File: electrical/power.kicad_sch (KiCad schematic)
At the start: 67 parts

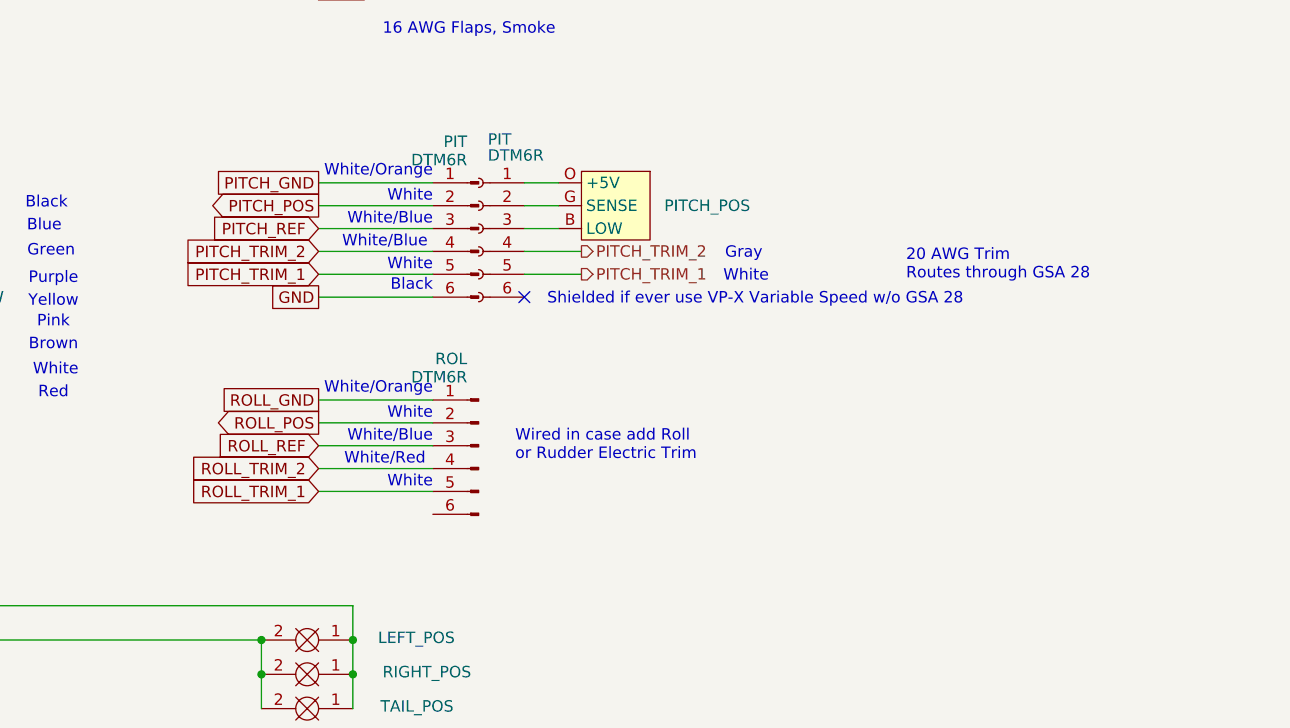
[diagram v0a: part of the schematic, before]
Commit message: Added Rudder Trim and Ray Allen T3 Servo Type.
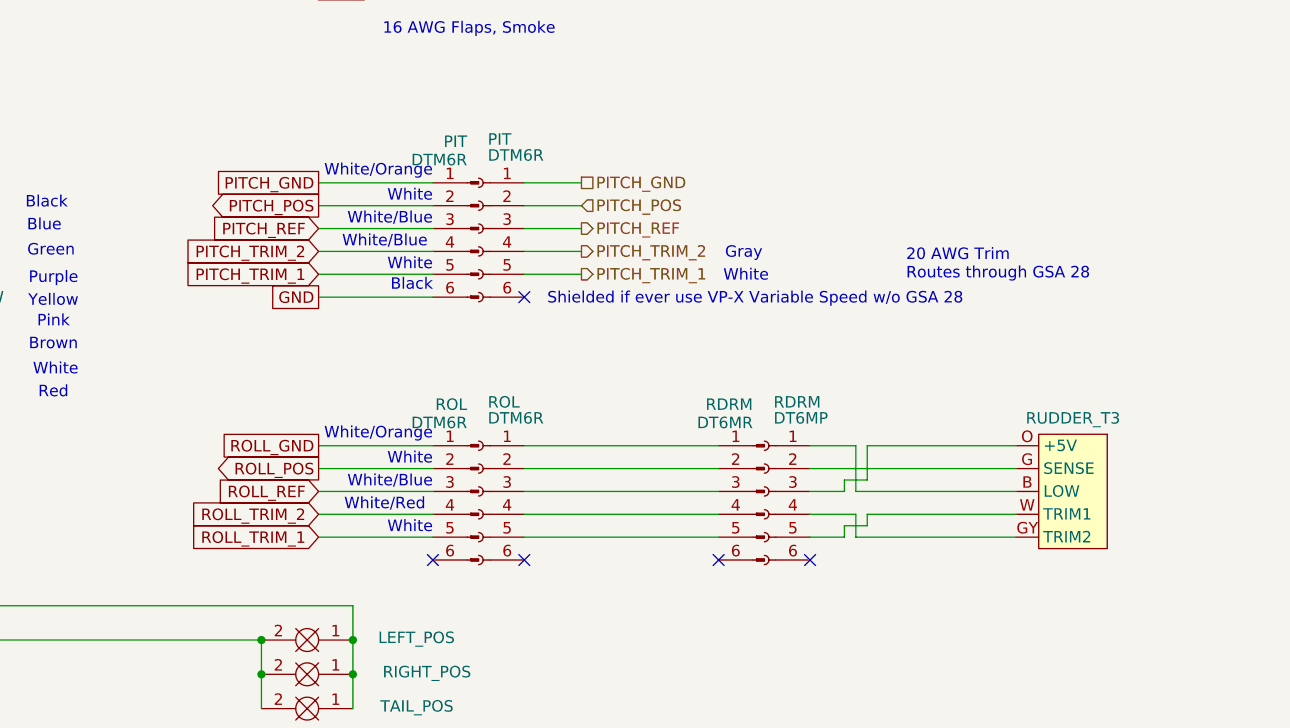
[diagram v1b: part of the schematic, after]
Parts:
- removed PITCH_POS: ~, symbol flyerx:Ray_Allen_POS-12
- added RDRM: DT6MR, symbol Connector:Conn_01x06_Pin
- added RDRM: DT6MP, symbol Connector:Conn_01x06_Socket
- added ROL: DTM6R, symbol Connector:Conn_01x06_Socket
- added RUDDER_T3: ~, symbol flyerx:Ray_Allen_T2/T3
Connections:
- net PITCH_GND: now also PIT.1 (Pin_1)
- net PITCH_POS: now also PIT.2 (Pin_2)
- net PITCH_REF: now also PIT.3 (Pin_3)
- new net: RDRM.1 (Pin_1), ROL.1 (Pin_1)
- new net: RDRM.2 (Pin_2), ROL.2 (Pin_2)
- new net: RDRM.3 (Pin_3), ROL.3 (Pin_3)
- new net: RDRM.4 (Pin_4), ROL.4 (Pin_4)
- new net: RDRM.5 (Pin_5), ROL.5 (Pin_5)
- new net: RDRM.1 (Pin_1), RUDDER_T3.B (LOW)
- new net: RDRM.2 (Pin_2), RUDDER_T3.G (SENSE)
- new net: RDRM.4 (Pin_4), RUDDER_T3.GY (TRIM2)
- new net: RDRM.3 (Pin_3), RUDDER_T3.O (+5V)
- new net: RDRM.5 (Pin_5), RUDDER_T3.W (TRIM1)
- no-connect marks 7 -> 11
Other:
- note removed: "Wired in case add Roll or Rudder Electric Trim"
- moved on the sheet: ROL

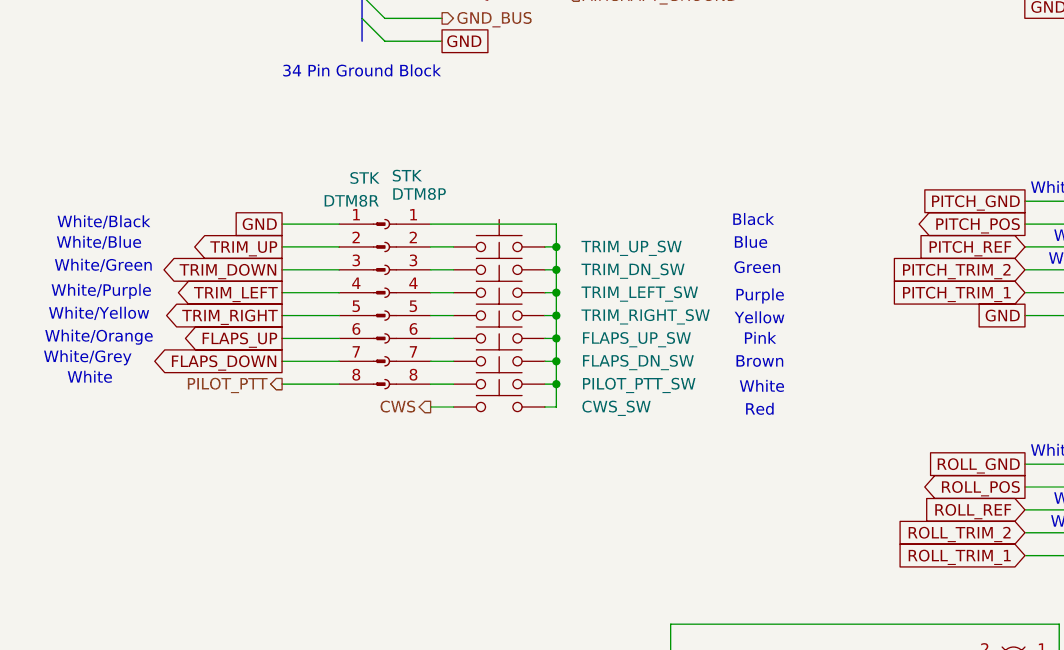
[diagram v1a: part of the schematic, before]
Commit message: Added connector to allow stick removal.
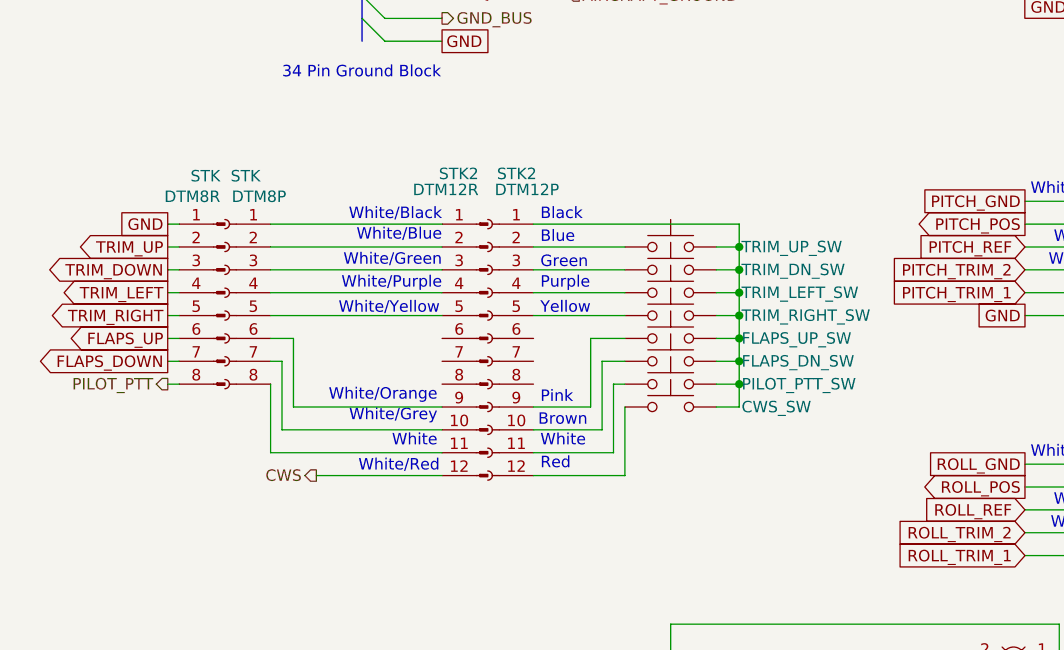
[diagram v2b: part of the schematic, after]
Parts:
- added STK2: DTM12R, symbol Connector:Conn_01x12_Pin
- added STK2: DTM12P, symbol Connector:Conn_01x12_Socket
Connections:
- net CWS: now also STK2.12 (Pin_12); no longer CWS_SW.1
- net at TRIM_UP_SW.1: now also STK2.2 (Pin_2); no longer STK.2 (Pin_2)
- net at CWS_SW.2, FLAPS_DN_SW.2, FLAPS_UP_SW.2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: now also STK2.1 (Pin_1); no longer STK.1 (Pin_1)
- net at TRIM_RIGHT_SW.1: now also STK2.5 (Pin_5); no longer STK.5 (Pin_5)
- net at FLAPS_DN_SW.1: now also STK2.10 (Pin_10); no longer STK.7 (Pin_7)
- net at TRIM_DN_SW.1: now also STK2.3 (Pin_3); no longer STK.3 (Pin_3)
- net at STK.6 (Pin_6): now also STK2.9 (Pin_9); no longer FLAPS_UP_SW.1
- net at STK.8 (Pin_8): now also STK2.11 (Pin_11); no longer PILOT_PTT_SW.1
- net at STK.4 (Pin_4): now also STK2.4 (Pin_4); no longer TRIM_LEFT_SW.1
- new net: CWS_SW.1, STK2.12 (Pin_12)
- new net: STK.1 (Pin_1), STK2.1 (Pin_1)
- new net: STK.7 (Pin_7), STK2.10 (Pin_10)
- new net: STK.2 (Pin_2), STK2.2 (Pin_2)
- new net: STK.3 (Pin_3), STK2.3 (Pin_3)
- new net: STK.5 (Pin_5), STK2.5 (Pin_5)
- new net: FLAPS_UP_SW.1, STK2.9 (Pin_9)
- new net: PILOT_PTT_SW.1, STK2.11 (Pin_11)
- new net: STK2.4 (Pin_4), TRIM_LEFT_SW.1
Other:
- moved on the sheet: CWS_SW, FLAPS_DN_SW, FLAPS_UP_SW, PILOT_PTT_SW, STK, TRIM_DN_SW, TRIM_LEFT_SW, TRIM_RIGHT_SW, TRIM_UP_SW

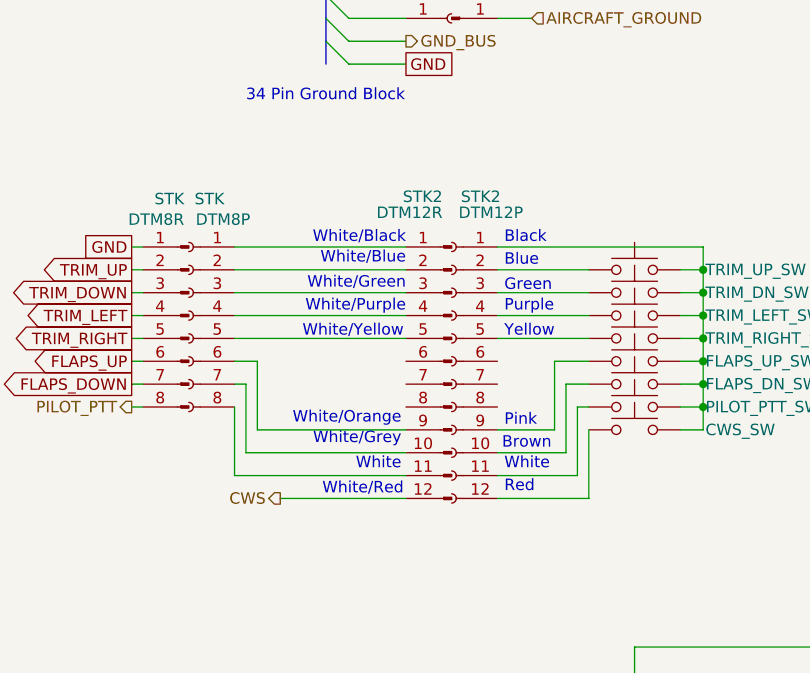
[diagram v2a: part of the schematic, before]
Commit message: Changed 12 connector to be populated in middle
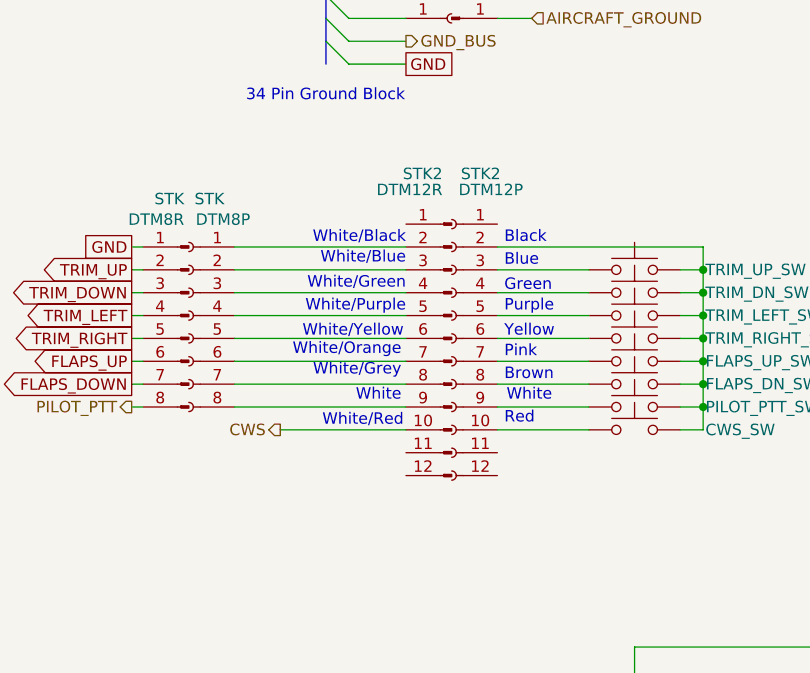
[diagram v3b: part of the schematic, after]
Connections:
- net CWS: now also STK2.10 (Pin_10); no longer STK2.12 (Pin_12)
- net at TRIM_UP_SW.1: now also STK2.3 (Pin_3); no longer STK2.2 (Pin_2)
- net at CWS_SW.2, FLAPS_DN_SW.2, FLAPS_UP_SW.2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: now also STK2.2 (Pin_2); no longer STK2.1 (Pin_1)
- net at CWS_SW.1: now also STK2.10 (Pin_10); no longer STK2.12 (Pin_12)
- net at TRIM_RIGHT_SW.1: now also STK2.6 (Pin_6); no longer STK2.5 (Pin_5)
- net at FLAPS_DN_SW.1: now also STK2.8 (Pin_8); no longer STK2.10 (Pin_10)
- net at TRIM_DN_SW.1: now also STK2.4 (Pin_4); no longer STK2.3 (Pin_3)
- net at STK2.1 (Pin_1): no longer STK.1 (Pin_1)
- net at STK.7 (Pin_7): now also STK2.8 (Pin_8); no longer STK2.10 (Pin_10)
- net at STK2.11 (Pin_11): no longer STK.8 (Pin_8)
- net at STK2.2 (Pin_2): now also STK.1 (Pin_1); no longer STK.2 (Pin_2)
- net at STK2.3 (Pin_3): now also STK.2 (Pin_2); no longer STK.3 (Pin_3)
- net at STK2.4 (Pin_4): now also STK.3 (Pin_3); no longer STK.4 (Pin_4)
- net at STK2.5 (Pin_5): now also STK.4 (Pin_4); no longer STK.5 (Pin_5)
- net at STK2.6 (Pin_6): now also STK.5 (Pin_5)
- net at STK2.7 (Pin_7): now also STK.6 (Pin_6)
- net at STK2.9 (Pin_9): now also STK.8 (Pin_8); no longer STK.6 (Pin_6)
- net at FLAPS_UP_SW.1: now also STK2.7 (Pin_7); no longer STK2.9 (Pin_9)
- net at PILOT_PTT_SW.1: now also STK2.9 (Pin_9); no longer STK2.11 (Pin_11)
- net at TRIM_LEFT_SW.1: now also STK2.5 (Pin_5); no longer STK2.4 (Pin_4)
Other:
- moved on the sheet: STK2
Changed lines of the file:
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@@
 	(text "Pink"
 		(exclude_from_sim no)
-		(at 68.072 297.434 0)
+		(at 68.072 289.814 0)
 		(effects
 			(font
@@
 	(text "White/Grey"
 		(exclude_from_sim no)
-		(at 56.642 299.466 0)
+		(at 56.642 291.846 0)
 		(effects
 			(font
@@
 	(text "White/Red"
 		(exclude_from_sim no)
-		(at 56.896 305.054 0)
+		(at 56.896 297.434 0)
 		(effects
 			(font
@@
 	(text "White"
 		(exclude_from_sim no)
-		(at 68.072 302.26 0)
+		(at 68.326 294.64 0)
 		(effects
 			(font
@@
 	(text "Brown"
 		(exclude_from_sim no)
-		(at 67.818 299.974 0)
+		(at 68.072 292.354 0)
 		(effects
 			(font
@@
 	(text "Red"
 		(exclude_from_sim no)
-		(at 68.072 304.8 0)
+		(at 68.072 297.18 0)
 		(effects
 			(font
@@
 	(text "White/Orange"
 		(exclude_from_sim no)
-		(at 56.642 297.18 0)
+		(at 56.642 289.56 0)
 		(effects
 			(font
@@
 	(text "White"
 		(exclude_from_sim no)
-		(at 56.642 302.26 0)
+		(at 56.642 294.64 0)
 		(effects
 			(font
@@
 	(wire
 		(pts
-			(xy 57.15 303.53) (xy 38.1 303.53)
+			(xy 57.15 295.91) (xy 38.1 295.91)
 		)
 		(stroke
@@
 	(wire
 		(pts
-			(xy 67.31 298.45) (xy 73.66 298.45)
+			(xy 67.31 290.83) (xy 77.47 290.83)
 		)
 		(stroke
@@
 	(wire
 		(pts
-			(xy 40.64 298.45) (xy 40.64 290.83)
-		)
-		(stroke
-			(width 0)
-			(type default)
-		)
-	)
-	(wire
-		(pts
-			(xy 67.31 306.07) (xy 77.47 306.07)
+			(xy 67.31 298.45) (xy 77.47 298.45)
 		)
 		(stroke
@@
 	(wire
 		(pts
-			(xy 77.47 306.07) (xy 77.47 298.45)
-		)
-		(stroke
-			(width 0)
-			(type default)
-		)
-	)
-	(wire
-		(pts
-			(xy 76.2 303.53) (xy 76.2 295.91)
-		)
-		(stroke
-			(width 0)
-			(type default)
-		)
-	)
-	(wire
-		(pts
 			(xy 165.1 208.28) (xy 215.9 208.28)
 		)
@@
 	(wire
 		(pts
-			(xy 74.93 293.37) (xy 77.47 293.37)
-		)
-		(stroke
-			(width 0)
-			(type default)
-		)
-	)
-	(wire
-		(pts
 			(xy 199.39 250.19) (xy 212.09 250.19)
 		)
@@
 	(wire
 		(pts
-			(xy 38.1 303.53) (xy 38.1 295.91)
-		)
-		(stroke
-			(width 0)
-			(type default)
-		)
-	)
-	(wire
-		(pts
-			(xy 67.31 303.53) (xy 76.2 303.53)
+			(xy 67.31 295.91) (xy 77.47 295.91)
 		)
 		(stroke
@@
 	(wire
 		(pts
-			(xy 40.64 290.83) (xy 38.1 290.83)
+			(xy 38.1 290.83) (xy 57.15 290.83)
 		)
 		(stroke
@@
 	(wire
 		(pts
-			(xy 39.37 293.37) (xy 38.1 293.37)
+			(xy 38.1 293.37) (xy 57.15 293.37)
 		)
 		(stroke
@@
 	(wire
 		(pts
-			(xy 76.2 295.91) (xy 77.47 295.91)
-		)
-		(stroke
-			(width 0)
-			(type default)
-		)
-	)
-	(wire
-		(pts
 			(xy 167.64 85.09) (xy 167.64 82.55)
 		)
@@
 	(wire
 		(pts
-			(xy 57.15 298.45) (xy 40.64 298.45)
-		)
-		(stroke
-			(width 0)
-			(type default)
-		)
-	)
-	(wire
-		(pts
 			(xy 175.26 248.92) (xy 175.26 246.38)
 		)
@@
 	(wire
 		(pts
-			(xy 74.93 300.99) (xy 74.93 293.37)
-		)
-		(stroke
-			(width 0)
-			(type default)
-		)
-	)
-	(wire
-		(pts
-			(xy 57.15 300.99) (xy 39.37 300.99)
-		)
-		(stroke
-			(width 0)
-			(type default)
-		)
-	)
-	(wire
-		(pts
 			(xy 165.1 213.36) (xy 185.42 213.36)
 		)
@@
 	(wire
 		(pts
-			(xy 43.18 306.07) (xy 57.15 306.07)
+			(xy 43.18 298.45) (xy 57.15 298.45)
 		)
 		(stroke
@@
 	(wire
 		(pts
-			(xy 67.31 300.99) (xy 74.93 300.99)
+			(xy 67.31 293.37) (xy 77.47 293.37)
 		)
 		(stroke
@@
 	(wire
 		(pts
-			(xy 73.66 298.45) (xy 73.66 290.83)
-		)
-		(stroke
-			(width 0)
-			(type default)
-		)
-	)
-	(wire
-		(pts
 			(xy 152.4 124.46) (xy 162.56 124.46)
 		)
@@
 	(wire
 		(pts
-			(xy 73.66 290.83) (xy 77.47 290.83)
-		)
-		(stroke
-			(width 0)
-			(type default)
-		)
-	)
-	(wire
-		(pts
 			(xy 157.48 133.35) (xy 162.56 133.35)
 		)
@@
 	(wire
 		(pts
-			(xy 39.37 300.99) (xy 39.37 293.37)
-		)
-		(stroke
-			(width 0)
-			(type default)
-		)
-	)
-	(wire
-		(pts
 			(xy 57.15 125.73) (xy 63.5 125.73)
 		)
@@
 	(hierarchical_label "CWS"
 		(shape output)
-		(at 43.18 306.07 180)
+		(at 43.18 298.45 180)
 		(effects
 			(font
@@
 	(symbol
 		(lib_id "Connector:Conn_01x12_Pin")
-		(at 62.23 290.83 0)
+		(at 62.23 288.29 0)
 		(mirror y)
 		(unit 1)
@@
 		(dnp no)
 		(property "Reference" "STK2"
-			(at 61.214 272.542 0)
+			(at 61.214 270.002 0)
 			(effects
 				(font
@@
 		)
 		(property "Value" "DTM12R"
-			(at 61.214 274.32 0)
+			(at 61.214 271.78 0)
 			(effects
 				(font
@@
 		)
 		(property "Footprint" ""
-			(at 62.23 290.83 0)
+			(at 62.23 288.29 0)
 			(effects
 				(font
@@
 		)
 		(property "Datasheet" "~"
-			(at 62.23 290.83 0)
+			(at 62.23 288.29 0)
 			(effects
 				(font
@@
 		)
 		(property "Description" "Generic connector, single row, 01x12, script generated"
-			(at 62.23 290.83 0)
+			(at 62.23 288.29 0)
 			(effects
 				(font
@@
 		)
 		(instances
-			(project ""
+			(project "electrical"
 				(path "/e8ec215a-dbe2-4eba-a577-e50a0a128049/2852c073-fbc9-4469-a6bf-ba3e911c7f5a"
 					(reference "STK2")
@@
 	(symbol
 		(lib_id "Connector:Conn_01x12_Socket")
-		(at 62.23 290.83 0)
+		(at 62.23 288.29 0)
 		(mirror y)
 		(unit 1)
@@
 		(dnp no)
 		(property "Reference" "STK2"
-			(at 63.246 272.542 0)
+			(at 63.246 270.002 0)
 			(effects
 				(font
@@
 		)
 		(property "Value" "DTM12P"
-			(at 62.992 274.32 0)
+			(at 62.992 271.78 0)
 			(effects
 				(font
@@
 		)
 		(property "Footprint" ""
-			(at 62.23 290.83 0)
+			(at 62.23 288.29 0)
 			(effects
 				(font
@@
 		)
 		(property "Datasheet" "~"
-			(at 62.23 290.83 0)
+			(at 62.23 288.29 0)
 			(effects
 				(font
@@
 		)
 		(property "Description" "Generic connector, single row, 01x12, script generated"
-			(at 62.23 290.83 0)
+			(at 62.23 288.29 0)
 			(effects
 				(font
@@
 		)
 		(instances
-			(project ""
+			(project "electrical"
 				(path "/e8ec215a-dbe2-4eba-a577-e50a0a128049/2852c073-fbc9-4469-a6bf-ba3e911c7f5a"
 					(reference "STK2")
